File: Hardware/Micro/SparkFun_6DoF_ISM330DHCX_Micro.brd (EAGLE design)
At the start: 20.3 x 12.7 mm, 45 parts, among them U1 ISM330DHCX

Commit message: Updates labels on Qwiic Micro, Updates IC on Qwiic Micro and Micro
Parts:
- moved JP3 5.08 mm to (6.35, 11.4)
- moved ADDR 5.08 mm to (16.8, 5.28)
- moved LED 5.08 mm to (19.2, 6.07)
- moved R6 5.08 mm to (16.5, 4.34)
- moved U$1 5.08 mm to (10.1, 6.30)
- moved U$13 5.08 mm to (14.2, 4.90)
- moved U$37 5.08 mm to (13.9, 3.25)
- moved C3 5.08 mm to (9.11, 8.20)
- moved C4 5.08 mm to (11.4, 8.81)
- moved D1 5.08 mm to (19.5, 6.35)
- moved FD1 5.08 mm to (5.56, 8.89)
- moved FD2 5.08 mm to (17.8, 2.39)
- moved FID1 5.08 mm to (5.56, 8.89)
- moved FID2 5.08 mm to (17.8, 2.39)
- moved I2C_PU 5.08 mm to (5.49, 6.35)
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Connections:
- net SDA renamed SDA/PICO
- net SDI_AUX renamed PICO_AUX
- net SDO/SA0 renamed POCI/SA0
- net SDO_AUX renamed POCI_AUX
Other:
- board text added: "Units in Inches"

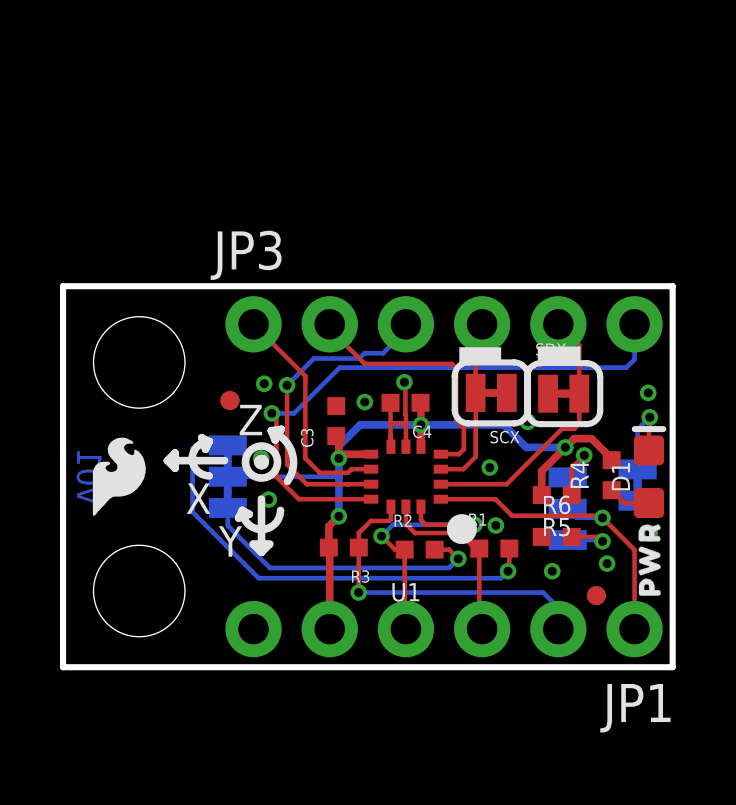
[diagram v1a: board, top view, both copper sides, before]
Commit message: Fixes labels, realigns the SDX jumper on top
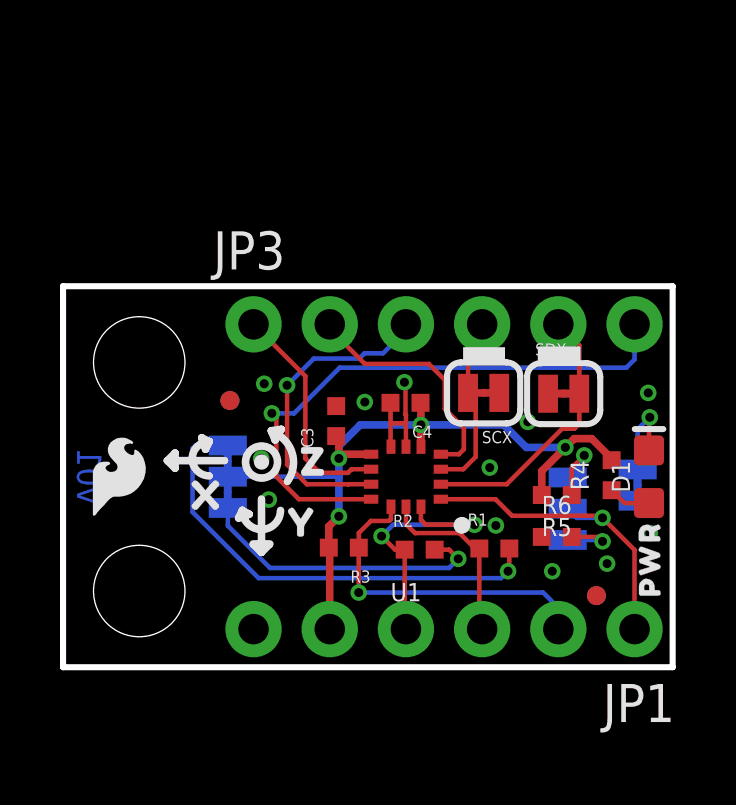
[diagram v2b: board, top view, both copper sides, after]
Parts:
- added U$3: (no value), ISMTopMini:X2114
- added U$4: (no value), ISMTopMini:Y2115
- added U$5: (no value), ISMTopMini:Z2116
- moved SCX 0.25 mm to (14.0, 9.14)
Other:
- board text removed: "X"
- board text removed: "Y"
- board text removed: "Z"
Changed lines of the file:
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@@
 <layer number="39" name="tKeepout" color="4" fill="11" visible="no" active="yes"/>
 <layer number="40" name="bKeepout" color="1" fill="11" visible="no" active="yes"/>
-<layer number="41" name="tRestrict" color="4" fill="10" visible="no" active="yes"/>
+<layer number="41" name="tRestrict" color="4" fill="10" visible="yes" active="yes"/>
 <layer number="42" name="bRestrict" color="1" fill="10" visible="no" active="yes"/>
 <layer number="43" name="vRestrict" color="2" fill="10" visible="no" active="yes"/>
@@
 <wire x1="4.6228" y1="7.648575" x2="4.7498" y2="7.267575" width="0.254" layer="21"/>
 <wire x1="3.7338" y1="7.140575" x2="3.7338" y2="6.632575" width="0.254" layer="21"/>
-<text x="5.197475" y="3.683" size="1.016" layer="21" font="vector" ratio="15" rot="SR0">Y</text>
-<text x="4.086225" y="5.11175" size="1.016" layer="21" font="vector" ratio="15" rot="SR0">X</text>
-<text x="5.832475" y="7.731125" size="1.016" layer="21" font="vector" ratio="15" rot="SR0">Z</text>
 <wire x1="6.94055" y1="7.883525" x2="7.273925" y2="7.93115" width="0.254" layer="21"/>
 <wire x1="6.94055" y1="7.883525" x2="7.06755" y2="7.57555" width="0.254" layer="21"/>
@@
 <circle x="6.6167" y="6.83895" radius="0.5334" width="0.254" layer="21"/>
 <rectangle x1="15.8242" y1="10.16" x2="17.2466" y2="10.6934" layer="21" rot="R180"/>
-<rectangle x1="13.208" y1="10.16" x2="14.605" y2="10.668" layer="21" rot="R180"/>
-<rectangle x1="11.176" y1="12.2936" x2="11.2268" y2="12.4968" layer="41"/>
-<rectangle x1="14.6812" y1="15.0876" x2="16.1544" y2="15.2908" layer="41"/>
-<wire x1="18.2372" y1="7.1628" x2="17.9832" y2="7.4168" width="0.1524" layer="22"/>
-<wire x1="17.9832" y1="7.4168" x2="15.6464" y2="7.4168" width="0.1524" layer="22"/>
+<rectangle x1="13.335" y1="10.16" x2="14.732" y2="10.668" layer="21" rot="R180"/>
+<rectangle x1="11.176" y1="7.0866" x2="11.2268" y2="7.2898" layer="41"/>
 <rectangle x1="15.3924" y1="7.1628" x2="15.9004" y2="7.6708" layer="22"/>
-<circle x="18.1864" y="7.2136" radius="0.14368125" width="0" layer="22"/>
 <dimension x1="20.32" y1="12.7" x2="0" y2="12.7" x3="10.16" y3="19.05" textsize="1.778" layer="47" dtype="horizontal" unit="inch"/>
 <dimension x1="0" y1="12.7" x2="0" y2="0" x3="-8.89" y3="6.35" textsize="1.778" layer="47" dtype="horizontal" unit="inch"/>
@@
 <dimension x1="11.43" y1="6.35" x2="11.43" y2="0" x3="27.94" y3="3.175" textsize="1.778" layer="47" dtype="horizontal" unit="inch"/>
 <text x="0" y="-3.81" size="1.778" layer="47" font="vector">Units in Inches</text>
+<wire x1="18.1356" y1="7.2644" x2="17.9832" y2="7.4168" width="0.508" layer="22"/>
+<wire x1="17.9832" y1="7.4168" x2="15.9004" y2="7.4168" width="0.508" layer="22"/>
 </plain>
 <attributes>
@@
 <attribute name="VALUE" x="15.7353" y="7.4676" size="0.4064" layer="27"/>
 </element>
-<element name="SCX" library="SparkFun-Jumpers" package="SMT-JUMPER_2_NC_TRACE_SILK" package3d_urn="urn:adsk.eagle:package:39281/1" value="JUMPER-SMT_2_NC_TRACE_SILK" x="14.2748" y="9.144" smashed="yes" rot="R180">
-<attribute name="NAME" x="15.2273" y="7.874" size="0.4064" layer="25" rot="R180"/>
-<attribute name="VALUE" x="15.2273" y="10.795" size="0.4064" layer="27" rot="R180"/>
+<element name="SCX" library="SparkFun-Jumpers" package="SMT-JUMPER_2_NC_TRACE_SILK" package3d_urn="urn:adsk.eagle:package:39281/1" value="JUMPER-SMT_2_NC_TRACE_SILK" x="14.0208" y="9.144" smashed="yes" rot="R180">
+<attribute name="NAME" x="14.9733" y="7.874" size="0.4064" layer="25" rot="R180"/>
+<attribute name="VALUE" x="14.9733" y="10.795" size="0.4064" layer="27" rot="R180"/>
 </element>
 <element name="JP3" library="SparkFun-Connectors" package="1X06_NO_SILK" value="IO" x="6.35" y="11.43" smashed="yes">
@@
 <element name="U$1" library="ISMTopMini" package="ISM330DHCX2115" value="" x="10.1092" y="6.2992" smashed="yes" rot="MR270"/>
 <element name="U$2" library="ISMTopMini" package="6DOF2115" value="" x="7.7724" y="6.35" smashed="yes" rot="MR270"/>
+<element name="U$3" library="ISMTopMini" package="X2114" value="" x="4.826" y="5.715" smashed="yes"/>
+<element name="U$4" library="ISMTopMini" package="Y2115" value="" x="8.001" y="4.826" smashed="yes"/>
+<element name="U$5" library="ISMTopMini" package="Z2116" value="" x="8.382" y="6.858" smashed="yes"/>
 </elements>
 <signals>
@@
 <via x="18.1356" y="3.4544" extent="1-16" drill="0.3"/>
 <via x="19.558" y="4.4704" extent="1-16" drill="0.3"/>
-<wire x1="10.93" y1="7.35" x2="10.93" y2="7.62" width="0.1524" layer="1"/>
-<wire x1="10.93" y1="7.62" x2="10.93" y2="7.7296" width="0.1524" layer="1"/>
 <via x="6.858" y="5.588" extent="1-16" drill="0.3"/>
 <via x="6.604" y="6.9596" extent="1-16" drill="0.3"/>
 <wire x1="11.43" y1="7.35" x2="11.43" y2="8.1327" width="0.1524" layer="1"/>
-<wire x1="11.43" y1="8.41373125" x2="11.4141" y2="8.42963125" width="0.1524" layer="1"/>
-<wire x1="11.4141" y1="9.4139" x2="11.3792" y2="9.4488" width="0.1524" layer="1"/>
-<wire x1="11.4141" y1="8.42963125" x2="11.4141" y2="9.4139" width="0.1524" layer="1"/>
+<wire x1="11.4141" y1="8.42963125" x2="11.43" y2="8.41373125" width="0.1524" layer="1"/>
 <via x="11.3792" y="9.4996" extent="1-16" drill="0.3"/>
-<wire x1="10.93" y1="7.62" x2="10.9173" y2="7.6327" width="0.1524" layer="1"/>
-<wire x1="10.9173" y1="8.1327" x2="10.9173" y2="7.6327" width="0.1524" layer="1"/>
 <wire x1="10.9173" y1="8.1327" x2="11.43" y2="8.1327" width="0.1524" layer="1"/>
 <wire x1="11.43" y1="8.1327" x2="11.43" y2="8.41373125" width="0.1524" layer="1"/>
@@
 <via x="14.224" y="6.6548" extent="1-16" drill="0.3"/>
 <via x="14.4272" y="4.7244" extent="1-16" drill="0.3"/>
+<wire x1="10.93" y1="7.35" x2="10.9173" y2="7.3627" width="0.1524" layer="1"/>
+<wire x1="10.9173" y1="7.3627" x2="10.9173" y2="8.1327" width="0.1524" layer="1"/>
+<wire x1="11.3792" y1="9.4996" x2="11.4141" y2="9.4647" width="0.1524" layer="1"/>
+<wire x1="11.4141" y1="9.4647" x2="11.4141" y2="8.42963125" width="0.1524" layer="1"/>
 </signal>
 <signal name="SCL">
@@
 <contactref element="SCX" pad="2"/>
 <contactref element="U1" pad="P3"/>
-<wire x1="13.7541" y1="7.0104" x2="13.7541" y2="9.144" width="0.1524" layer="1"/>
-<wire x1="13.7541" y1="9.144" x2="13.7541" y2="11.2141" width="0.1524" layer="1"/>
-<wire x1="13.7541" y1="11.2141" x2="13.97" y2="11.43" width="0.1524" layer="1"/>
+<wire x1="13.7541" y1="8.89" x2="13.7541" y2="7.0104" width="0.1524" layer="1"/>
+<wire x1="13.7541" y1="8.89" x2="13.5001" y2="9.144" width="0.1524" layer="1"/>
+<wire x1="13.5001" y1="9.144" x2="13.5001" y2="10.9601" width="0.1524" layer="1"/>
+<wire x1="13.5001" y1="10.9601" x2="13.97" y2="11.43" width="0.1524" layer="1"/>
 <wire x1="12.5925" y1="6.6" x2="13.3437" y2="6.6" width="0.1524" layer="1"/>
 <wire x1="13.3437" y1="6.6" x2="13.7541" y2="7.0104" width="0.1524" layer="1"/>
@@
 <wire x1="12.5925" y1="7.1" x2="13.196" y2="7.1" width="0.1524" layer="1"/>
 <wire x1="13.196" y1="7.1" x2="13.3604" y2="7.2644" width="0.1524" layer="1"/>
-<wire x1="12.954" y1="10.1092" x2="10.0584" y2="10.1092" width="0.1524" layer="1"/>
-<wire x1="13.1064" y1="9.9568" x2="12.954" y2="10.1092" width="0.1524" layer="1"/>
+<wire x1="12.192" y1="10.1092" x2="10.0584" y2="10.1092" width="0.1524" layer="1"/>
 <wire x1="13.3604" y1="7.2644" x2="13.3604" y2="7.9756" width="0.1524" layer="1"/>
-<wire x1="13.3604" y1="7.9756" x2="13.1064" y2="8.2296" width="0.1524" layer="1"/>
-<wire x1="13.1064" y1="8.2296" x2="13.1064" y2="9.9568" width="0.1524" layer="1"/>
+<wire x1="13.3604" y1="7.9756" x2="12.7254" y2="8.6106" width="0.1524" layer="1"/>
 <wire x1="10.0584" y1="10.1092" x2="8.89" y2="11.2776" width="0.1524" layer="1"/>
 <wire x1="8.89" y1="11.2776" x2="8.89" y2="11.43" width="0.1524" layer="1"/>
+<wire x1="12.7254" y1="9.5758" x2="12.192" y2="10.1092" width="0.1524" layer="1"/>
+<wire x1="12.7254" y1="8.6106" x2="12.7254" y2="9.5758" width="0.1524" layer="1"/>
 </signal>
 <signal name="INT2">
